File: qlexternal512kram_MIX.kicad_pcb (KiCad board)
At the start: 2 copper layers, 97.8 x 35.6 mm, 14 parts, among them J1 QL_SLOT_DIN41612_CARD, J2 QL_SLOT_DIN41612_CARD, U1 AS6C4008-55PCN, U2 GAL16V8, U3 LM1117-5.0

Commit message: Fix reference for IC
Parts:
- U1: value AS6C4008-55PCN -> HM628512BLFP-7
- U2: value GAL16V8 -> GAL16V8B-25QP
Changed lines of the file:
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@@
       (effects (font (size 1 1) (thickness 0.15)))
     )
-    (fp_text value "GAL16V8" (at 3.81 25.19 90) (layer "F.Fab")
+    (fp_text value "GAL16V8B-25QP" (at 3.81 25.19 90) (layer "F.Fab")
       (effects (font (size 1 1) (thickness 0.15)))
     )
@@
       (effects (font (size 1 1) (thickness 0.15)))
     )
-    (fp_text value "AS6C4008-55PCN" (at 0 11.2 90) (layer "F.Fab")
+    (fp_text value "HM628512BLFP-7" (at 0 11.2 90) (layer "F.Fab")
       (effects (font (size 1 1) (thickness 0.15)))
     )

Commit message: Updated info
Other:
- board text added: "00-512kB 10-256kB 10-192kB 11-128kB"
- board text added: "SINCLAIR QL 512kB RAM"
- board text added: "www.va-de-retro.com"
- board text removed: "0 0 - 512Kb 1 0 - 256kb 1 0 - 192Kb 1 1 - 128Kb"
- board text removed: "SINCLAIR QL 512Kb RAM"
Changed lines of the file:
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@@
     (property "Sheetname" "")
     (attr smd)
-    (fp_text reference "U3" (at 0 -4.5) (layer "F.SilkS")
+    (fp_text reference "U3" (at 0 -4.5 90) (layer "F.SilkS")
       (effects (font (size 1 1) (thickness 0.15)))
     )
@@
     (property "Sheetname" "")
     (attr through_hole)
-    (fp_text reference "J1" (at -83.82 1) (layer "F.SilkS")
+    (fp_text reference "J1" (at -83.82 1.27 90) (layer "F.SilkS")
       (effects (font (size 1 1) (thickness 0.15)))
     )
@@
     (property "Sheetname" "")
     (attr through_hole)
-    (fp_text reference "J2" (at 83.82 1) (layer "F.SilkS")
+    (fp_text reference "J2" (at 83.82 1.27 90) (layer "F.SilkS")
       (effects (font (size 1 1) (thickness 0.15)))
     )
@@
     (effects (font (size 1 1) (thickness 0.15)))
   )
-  (gr_text "0 0 - 512Kb\n1 0 - 256kb\n1 0 - 192Kb\n1 1 - 128Kb " (at 186.15 67.31 90) (layer "F.SilkS")
+  (gr_text "00-512kB\n10-256kB\n10-192kB\n11-128kB " (at 182.975 63.5) (layer "F.SilkS")
     (effects (font (size 1 0.8) (thickness 0.15)) (justify left))
   )
-  (gr_text "SINCLAIR QL\n512Kb RAM" (at 108.045 76.073) (layer "F.SilkS")
+  (gr_text "SINCLAIR QL\n512kB RAM" (at 108.045 76.073) (layer "F.SilkS")
     (effects (font (size 2 2) (thickness 0.3)))
   )
+  (gr_text "www.va-de-retro.com" (at 165.83 62.865) (layer "F.SilkS")
+    (effects (font (size 1 1) (thickness 0.15)))
+  )
   (gr_text "(C) 2022 Alvaro Alea Fdz" (at 166.846 77.597) (layer "F.SilkS")

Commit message: Update QL Conector
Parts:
- removed REF**: KiCad-Logo2_5mm_SilkScreen, Symbol:KiCad-Logo2_5mm_SilkScreen
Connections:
- J1 pad a1: +9V -> GND
- J1 pad a10: /A4 -> /A16
- J1 pad a11: /A5 -> /CLKCPU
- J1 pad a12: /A6 -> /RED
- J1 pad a13: /A7 -> /A14
- J1 pad a14: /A8 -> /A13
- J1 pad a15: /A9 -> /A12
- J1 pad a16: /A10 -> /A11
- J1 pad a17: /A11 -> /A10
- J1 pad a18: /A12 -> /A9
- J1 pad a19: /A13 -> /A8
- J1 pad a2: /me12v -> /D3
- J1 pad a20: /A14 -> /A7
- J1 pad a21: /RED -> /A6
- J1 pad a22: /CLKCPU -> /A5
- J1 pad a23: /A16 -> /A4
- J1 pad a24: /A17 -> /A3
- J1 pad a25: /A18 -> /DBG
- J1 pad a26: /A19 -> /SP2
- J1 pad a27: /D7 -> /DSMC
- J1 pad a28: /D6 -> /SP1
- J1 pad a29: /D5 -> /SP0
- J1 pad a3: /ma12v -> /D4
- J1 pad a30: /D4 -> /ma12v
- J1 pad a31: /D3 -> /me12v
- J1 pad a32: GND -> +9V
- J1 pad a4: /SP0 -> /D5
- J1 pad a5: /SP1 -> /D6
- J1 pad a6: /DSMC -> /D7
- J1 pad a7: /SP2 -> /A19
- J1 pad a8: /DBG -> /A18
- J1 pad a9: /A3 -> /A17
- J1 pad b1: +9V -> GND
- J1 pad b10: /ROMOE -> /BR
- J1 pad b11: /A0 -> /A15
- J1 pad b12: /FC0 -> /RESET
- J1 pad b13: /FC1 -> /CSYNC
- J1 pad b14: /FC2 -> /E
- J1 pad b15: /BLUE -> /VSYNC
- J1 pad b16: /GREEN -> /VPA
- J1 pad b17: /VPA -> /GREEN
- J1 pad b18: /VSYNC -> /BLUE
- J1 pad b19: /E -> /FC2
- J1 pad b2: +9V -> /D2
- J1 pad b20: /CSYNC -> /FC1
- J1 pad b21: /RESET -> /FC0
- J1 pad b22: /A15 -> /A0
- J1 pad b23: /BR -> /ROMOE
- J1 pad b24: /BG -> /A1
- J1 pad b25: /DTACK -> /A2
- J1 pad b26: /RW -> /SP3
- J1 pad b27: /DS -> /IPL0
- J1 pad b28: /AS -> /BERR
- J1 pad b29: /D0 -> /IPL1
- J1 pad b3: /EXTINT -> /D1
- J1 pad b30: /D1 -> /EXTINT
- J1 pad b31: /D2 -> +9V
- J1 pad b32: GND -> +9V
- J1 pad b4: /IPL1 -> /D0
- J1 pad b5: /BERR -> /AS
- J1 pad b6: /IPL0 -> /DS
- J1 pad b7: /SP3 -> /RW
- J1 pad b8: /A2 -> /DTACK
- J1 pad b9: /A1 -> /BG
- J2 pad a1: +9V -> GND
- J2 pad a10: /A4 -> /A16
- J2 pad a11: /A5 -> /CLKCPU
- J2 pad a12: /A6 -> /RED
- J2 pad a13: /A7 -> /A14
- J2 pad a14: /A8 -> /A13
- J2 pad a15: /A9 -> /A12
- J2 pad a16: /A10 -> /A11
- J2 pad a17: /A11 -> /A10
- J2 pad a18: /A12 -> /A9
- J2 pad a19: /A13 -> /A8
- J2 pad a2: /me12v -> /D3
- J2 pad a20: /A14 -> /A7
- J2 pad a21: /RED -> /A6
- J2 pad a22: /CLKCPU -> /A5
- J2 pad a23: /A16 -> /A4
- J2 pad a24: /A17 -> /A3
- J2 pad a25: /A18 -> /DBG
- J2 pad a26: /A19 -> /SP2
- J2 pad a27: /D7 -> /DSMC
- J2 pad a28: /D6 -> /SP1
- J2 pad a29: /D5 -> /SP0
- J2 pad a3: /ma12v -> /D4
- J2 pad a30: /D4 -> /ma12v
- J2 pad a31: /D3 -> /me12v
- J2 pad a32: GND -> +9V
- J2 pad a4: /SP0 -> /D5
- J2 pad a5: /SP1 -> /D6
- J2 pad a6: /DSMC -> /D7
- J2 pad a7: /SP2 -> /A19
- J2 pad a8: /DBG -> /A18
- J2 pad a9: /A3 -> /A17
- J2 pad b1: +9V -> GND
- J2 pad b10: /ROMOE -> /BR
- J2 pad b11: /A0 -> /A15
- J2 pad b12: /FC0 -> /RESET
- J2 pad b13: /FC1 -> /CSYNC
- J2 pad b14: /FC2 -> /E
- J2 pad b15: /BLUE -> /VSYNC
- J2 pad b16: /GREEN -> /VPA
- J2 pad b17: /VPA -> /GREEN
- J2 pad b18: /VSYNC -> /BLUE
- J2 pad b19: /E -> /FC2
- J2 pad b2: +9V -> /D2
- J2 pad b20: /CSYNC -> /FC1
- J2 pad b21: /RESET -> /FC0
- J2 pad b22: /A15 -> /A0
- J2 pad b23: /BR -> /ROMOE
- J2 pad b24: /BG -> /A1
- J2 pad b25: /DTACK -> /A2
- J2 pad b26: /RW -> /SP3
- J2 pad b27: /DS -> /IPL0
- J2 pad b28: /AS -> /BERR
- J2 pad b29: /D0 -> /IPL1
- J2 pad b3: /EXTINT -> /D1
- J2 pad b30: /D1 -> /EXTINT
- J2 pad b31: /D2 -> +9V
- J2 pad b32: GND -> +9V
- J2 pad b4: /IPL1 -> /D0
- J2 pad b5: /BERR -> /AS
- J2 pad b6: /IPL0 -> /DS
- J2 pad b7: /SP3 -> /RW
- J2 pad b8: /A2 -> /DTACK
- J2 pad b9: /A1 -> /BG

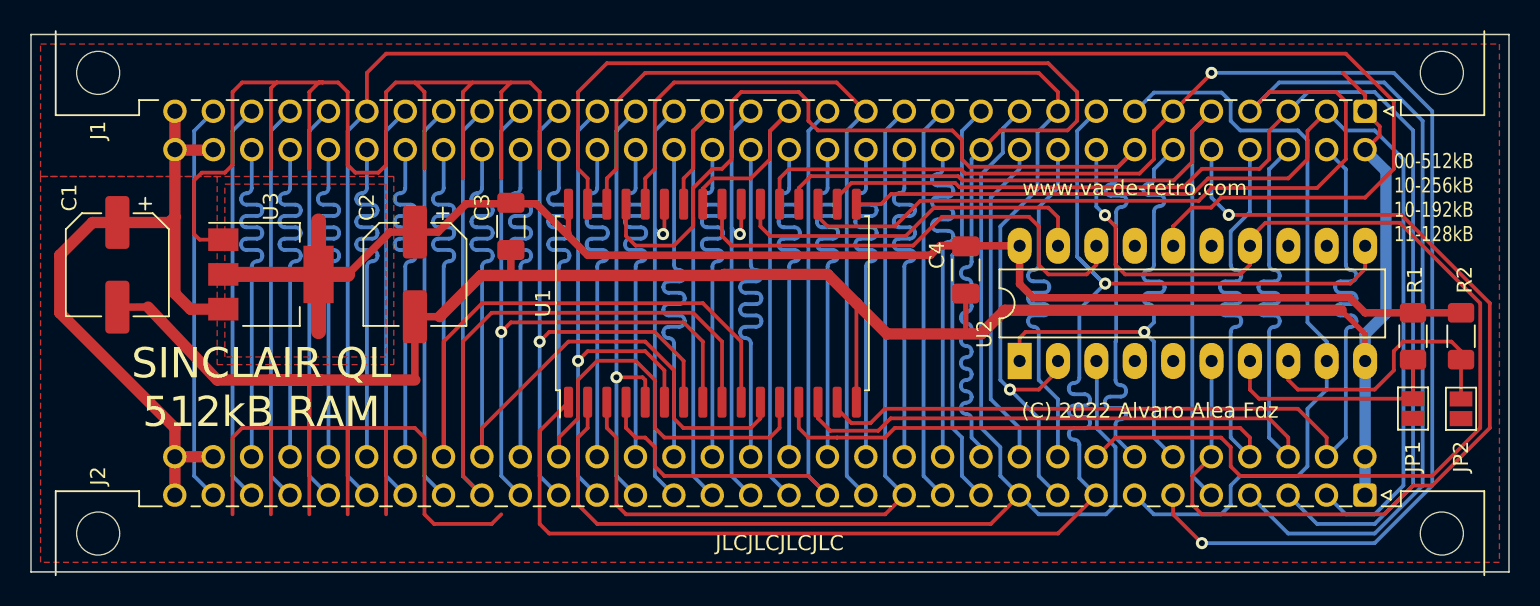
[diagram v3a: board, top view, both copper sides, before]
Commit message: Add compatibility with MiniTrump Card, and moved GAL to galasm
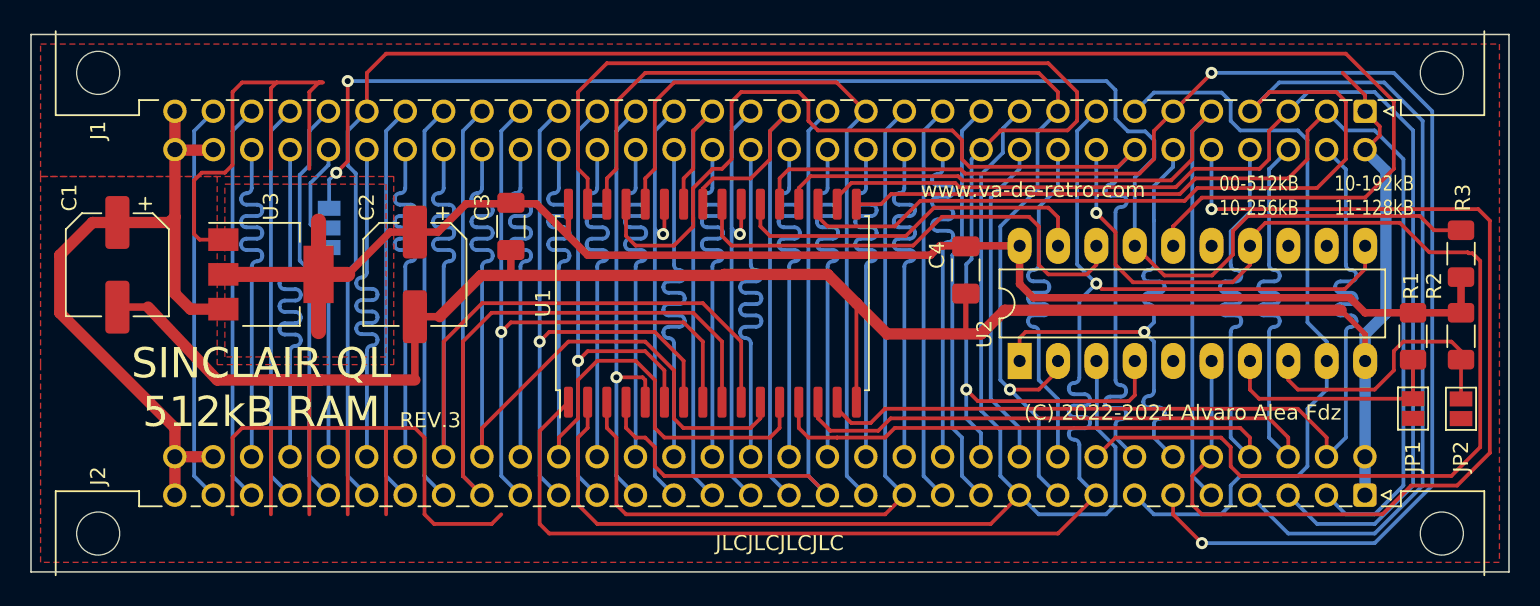
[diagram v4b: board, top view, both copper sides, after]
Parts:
- added JP3: Jumper_3_Open, Jumper:SolderJumper-3_P1.3mm_Open_Pad1.0x1.5mm, B.Cu at (112.5, 65.5)
- added R3: 10K, Resistor_SMD:R_1206_3216Metric_Pad1.30x1.75mm_HandSolder, F.Cu at (187.4, 67.2)
- C1: value 100u/16V -> 100u/25V
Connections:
- J2 pad b28: /BERR -> Net-(J2-~{BERR})
- U2 pad 17: unconnected-(U2-I03-Pad17) -> Net-(JP3-B)
- U2 pad 4: unconnected-(U2-I4-Pad4) -> /A15
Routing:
- net Net-(JP3-B): track 0.00 -> 97.9 mm, vias 0 -> 2
- net GND: track 278.1 -> 228.6 mm
- net /BERR: track 26.4 -> 6.74 mm
- net Net-(J2-~{BERR}): track 0.00 -> 13.8 mm
- net /A15: track 77.4 -> 87.2 mm, vias 0 -> 1
- net /AS: track 65.1 -> 69.7 mm
- net VCC: track 98.2 -> 100.6 mm
- net /DTACK: track 74.4 -> 76.8 mm
- net /A18: track 101.4 -> 99.4 mm
- net /D5: track 100.1 -> 99.2 mm
- net /A17: track 71.7 -> 71.1 mm
- net /SP1: track 26.4 -> 27.0 mm
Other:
- board text added: "(C) 2022-2024 Alvaro Alea Fdz"
- board text added: "00-512kB 10-256kB"
- board text added: "10-192kB 11-128kB"
- board text added: "REV.3"
- board text removed: "(C) 2022 Alvaro Alea Fdz"
- board text removed: "00-512kB 10-256kB 10-192kB 11-128kB"

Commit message: minor typos
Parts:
- J1: value QL_SLOT_DIN41612_CARD -> QL_SLOT_DIN41612_FEMALE-90degrees
- J2: value QL_SLOT_DIN41612_CARD -> QL_SLOT_DIN41612_MALE_90degrees
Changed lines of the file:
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@@
 			)
 		)
-		(property "Value" "QL_SLOT_DIN41612_CARD"
+		(property "Value" "QL_SLOT_DIN41612_FEMALE-90degrees"
 			(at -39.37 -7.62 0)
 			(layer "F.Fab")
@@
 			)
 		)
-		(property "Value" "QL_SLOT_DIN41612_CARD"
+		(property "Value" "QL_SLOT_DIN41612_MALE_90degrees"
 			(at 39.37 5.08 0)
 			(layer "F.Fab")
@@
 		)
 		(height 3.175)
-		(gr_text "3,8500 in"
+		(gr_text "97,7900 mm"
 			(at 141.6205 48.895 0)
 			(layer "Dwgs.User")
@@
 		)
 		(height -5.08)
-		(gr_text "1,4000 in"
+		(gr_text "35,5600 mm"
 			(at 195.04 70.485 90)
 			(layer "Dwgs.User")

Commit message: typo in skillscreen
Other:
- board text added: "00-512kB 01-256kB"
- board text removed: "00-512kB 10-256kB"
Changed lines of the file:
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@@
 		)
 	)
-	(gr_text "00-512kB\n10-256kB"
+	(gr_text "00-512kB\n01-256kB"
 		(at 171.418 63.373 0)
 		(layer "F.SilkS")
